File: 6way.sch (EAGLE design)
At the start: 10 parts

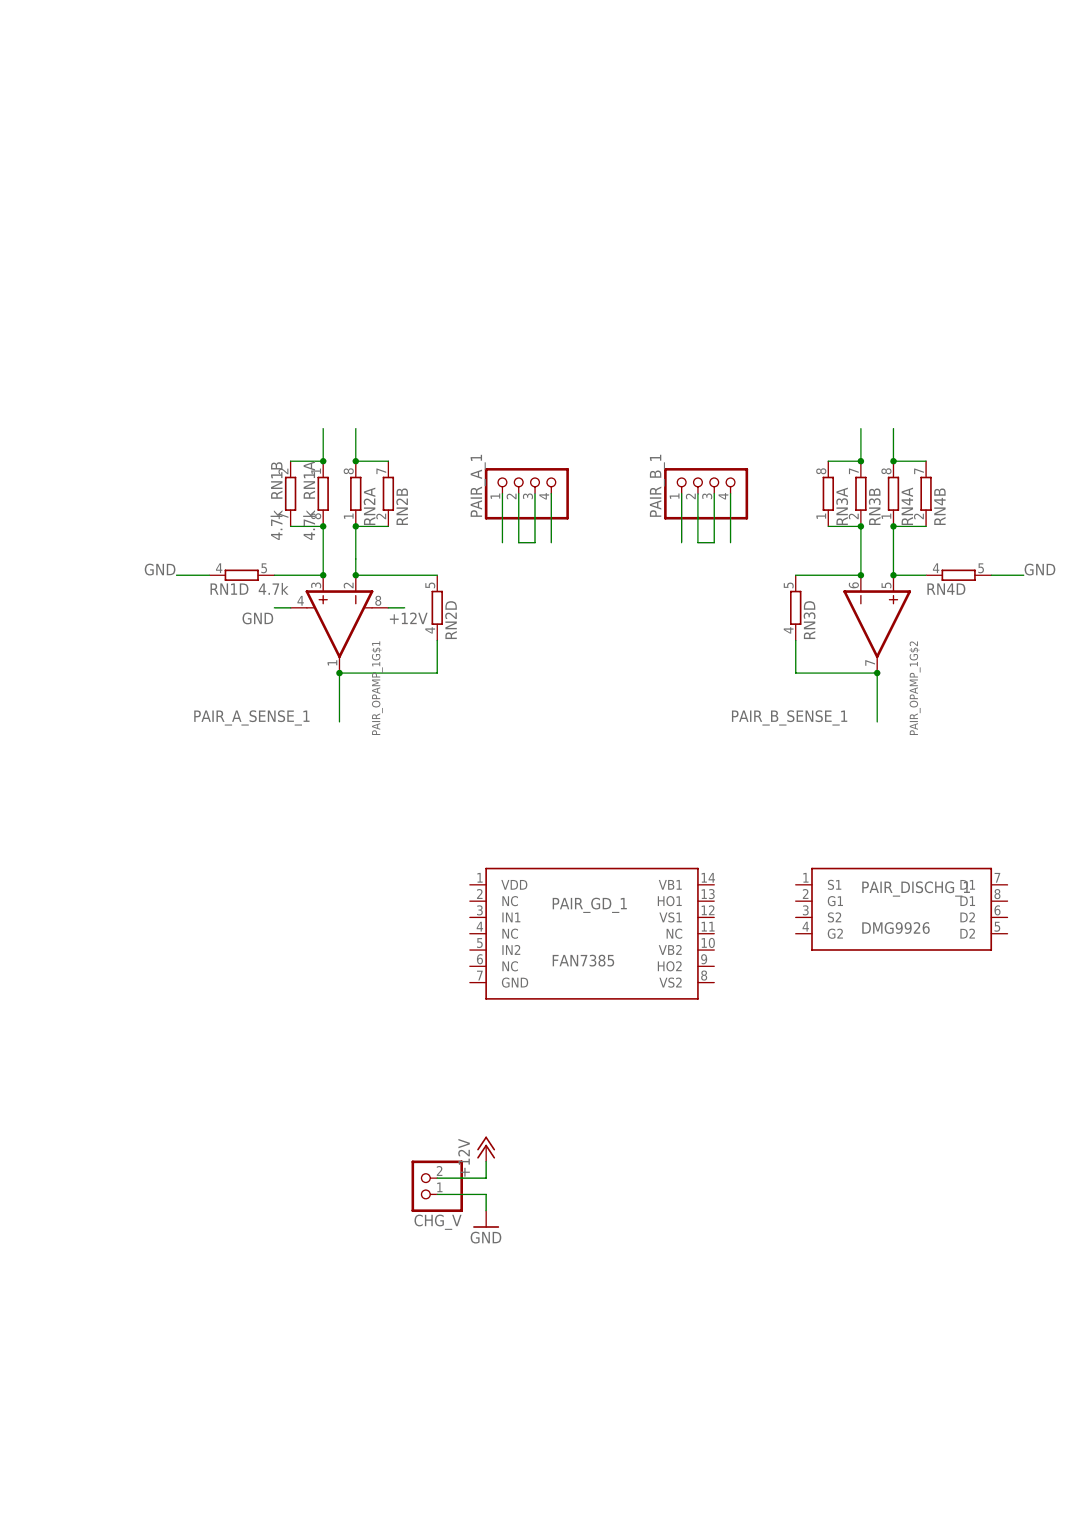
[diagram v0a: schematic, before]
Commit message: wired the signals that I know to handle, next up is figuring out the rest of it, datasheet is a bit sparse on details here
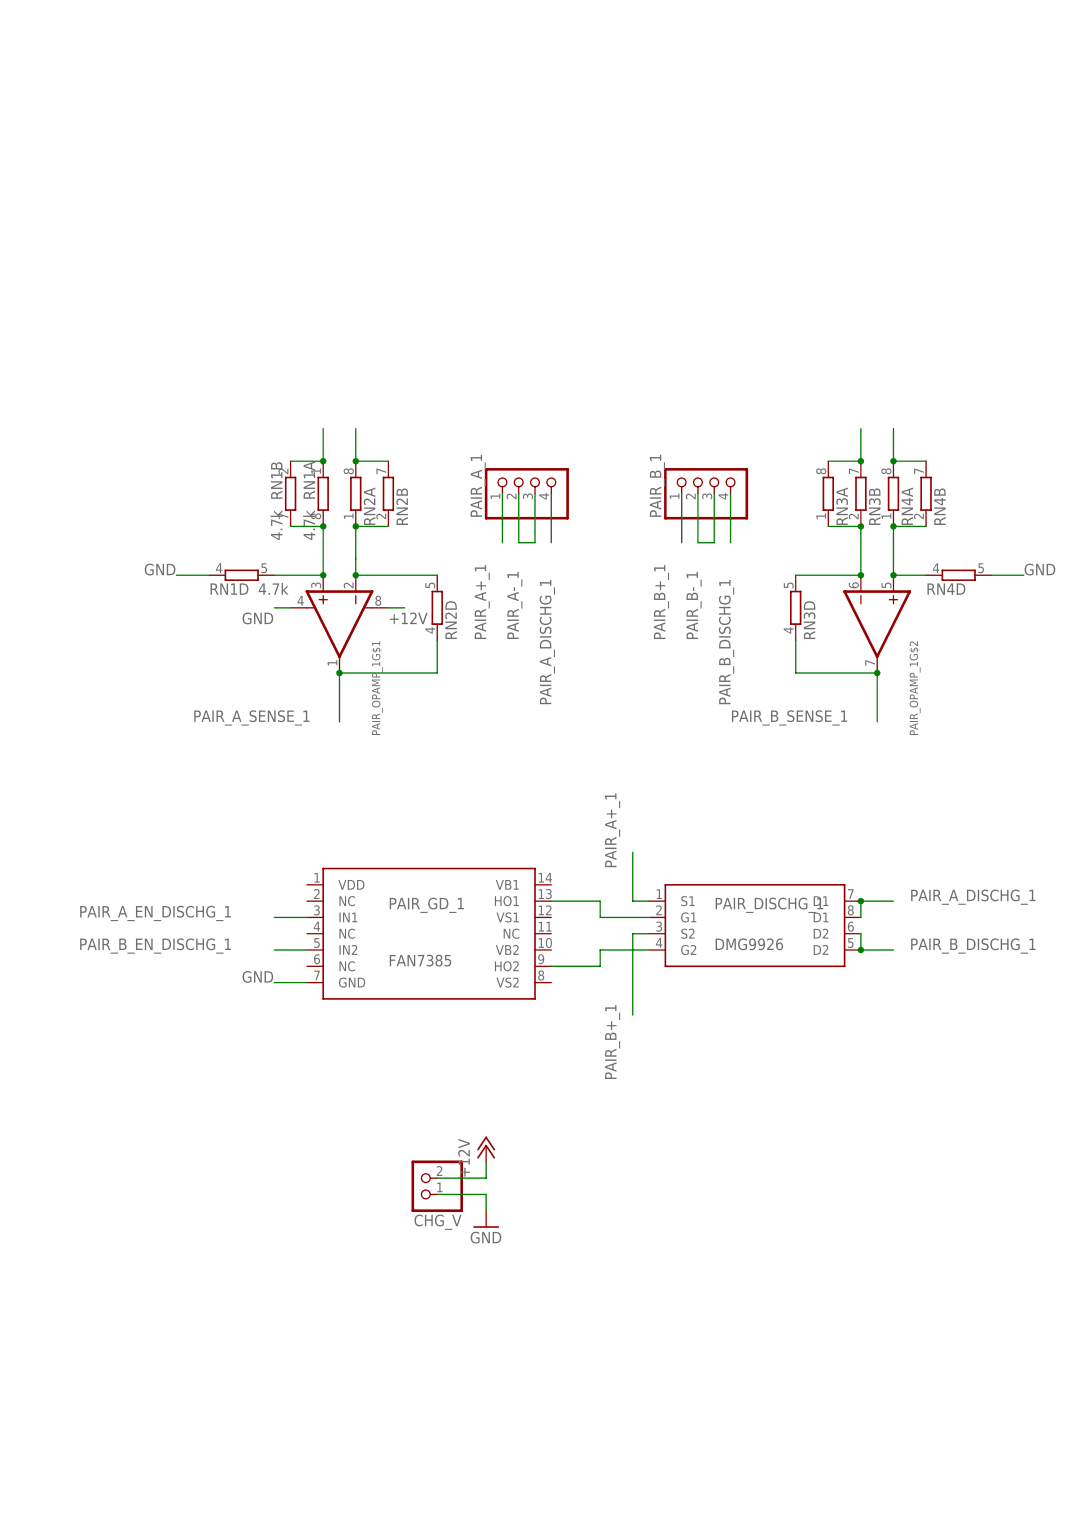
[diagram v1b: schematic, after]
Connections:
- new net N$4: PAIR_DISCHG_1.G1, PAIR_GD_1.HO1
- new net N$6: PAIR_DISCHG_1.G2, PAIR_GD_1.HO2
- new net PAIR_A_EN_DISCHG_1: PAIR_GD_1.IN1
- new net PAIR_B_EN_DISCHG_1: PAIR_GD_1.IN2
- net GND: now also PAIR_GD_1.GND
- net PAIR_A+_1: now also PAIR_DISCHG_1.S1
- net PAIR_A_DISCHG_1: now also PAIR_DISCHG_1.D1@1, PAIR_DISCHG_1.D1@2
- net PAIR_B+_1: now also PAIR_DISCHG_1.S2
- net PAIR_B_DISCHG_1: now also PAIR_DISCHG_1.D2@1, PAIR_DISCHG_1.D2@2
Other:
- moved on the sheet: PAIR_DISCHG_1, PAIR_GD_1
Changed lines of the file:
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@@
 <instance part="RN4" gate="D" x="86.36" y="101.6"/>
 <instance part="PAIR_B_1" gate="A" x="48.26" y="116.84" rot="R90"/>
-<instance part="PAIR_GD_1" gate="G$1" x="25.4" y="45.72"/>
-<instance part="PAIR_DISCHG_1" gate="G$1" x="73.66" y="50.8"/>
+<instance part="PAIR_GD_1" gate="G$1" x="0" y="45.72"/>
+<instance part="PAIR_DISCHG_1" gate="G$1" x="50.8" y="48.26"/>
 </instances>
 <busses>
@@
 <label x="96.52" y="101.6" size="1.778" layer="95"/>
 </segment>
+<segment>
+<pinref part="PAIR_GD_1" gate="G$1" pin="GND"/>
+<wire x1="-15.24" y1="38.1" x2="-20.32" y2="38.1" width="0.1524" layer="91"/>
+<label x="-25.4" y="38.1" size="1.778" layer="95"/>
+</segment>
 </net>
 <net name="PAIR_1_A_+" class="2">
@@
 <wire x1="20.32" y1="114.3" x2="20.32" y2="106.68" width="0.1524" layer="91"/>
 <wire x1="17.78" y1="106.68" x2="20.32" y2="106.68" width="0.1524" layer="91"/>
+<label x="17.78" y="91.44" size="1.778" layer="95" rot="R90"/>
 </segment>
 <segment>
@@
 <pinref part="PAIR_A_1" gate="A" pin="4"/>
 <wire x1="22.86" y1="114.3" x2="22.86" y2="106.68" width="0.1524" layer="91"/>
+<label x="22.86" y="81.28" size="1.778" layer="95" rot="R90"/>
+</segment>
+<segment>
+<pinref part="PAIR_DISCHG_1" gate="G$1" pin="D1@1"/>
+<pinref part="PAIR_DISCHG_1" gate="G$1" pin="D1@2"/>
+<wire x1="71.12" y1="48.26" x2="71.12" y2="50.8" width="0.1524" layer="91"/>
+<wire x1="71.12" y1="50.8" x2="76.2" y2="50.8" width="0.1524" layer="91"/>
+<junction x="71.12" y="50.8"/>
+<label x="78.74" y="50.8" size="1.778" layer="95"/>
 </segment>
 </net>
@@
 <pinref part="PAIR_A_1" gate="A" pin="1"/>
 <wire x1="15.24" y1="114.3" x2="15.24" y2="106.68" width="0.1524" layer="91"/>
+<label x="12.7" y="91.44" size="1.778" layer="95" rot="R90"/>
+</segment>
+<segment>
+<pinref part="PAIR_DISCHG_1" gate="G$1" pin="S1"/>
+<wire x1="38.1" y1="50.8" x2="35.56" y2="50.8" width="0.1524" layer="91"/>
+<wire x1="35.56" y1="50.8" x2="35.56" y2="58.42" width="0.1524" layer="91"/>
+<label x="33.02" y="55.88" size="1.778" layer="95" rot="R90"/>
 </segment>
 </net>
@@
 <wire x1="48.26" y1="114.3" x2="48.26" y2="106.68" width="0.1524" layer="91"/>
 <wire x1="45.72" y1="106.68" x2="48.26" y2="106.68" width="0.1524" layer="91"/>
+<label x="45.72" y="91.44" size="1.778" layer="95" rot="R90"/>
 </segment>
 <segment>
@@
 <pinref part="PAIR_B_1" gate="A" pin="4"/>
 <wire x1="50.8" y1="114.3" x2="50.8" y2="106.68" width="0.1524" layer="91"/>
+<label x="50.8" y="81.28" size="1.778" layer="95" rot="R90"/>
+</segment>
+<segment>
+<pinref part="PAIR_DISCHG_1" gate="G$1" pin="D2@1"/>
+<pinref part="PAIR_DISCHG_1" gate="G$1" pin="D2@2"/>
+<wire x1="71.12" y1="45.72" x2="71.12" y2="43.18" width="0.1524" layer="91"/>
+<wire x1="71.12" y1="43.18" x2="76.2" y2="43.18" width="0.1524" layer="91"/>
+<junction x="71.12" y="43.18"/>
+<label x="78.74" y="43.18" size="1.778" layer="95"/>
 </segment>
 </net>
@@
 <pinref part="PAIR_B_1" gate="A" pin="1"/>
 <wire x1="43.18" y1="114.3" x2="43.18" y2="106.68" width="0.1524" layer="91"/>
+<label x="40.64" y="91.44" size="1.778" layer="95" rot="R90"/>
 </segment>
 <segment>
@@
 <wire x1="76.2" y1="119.38" x2="76.2" y2="124.46" width="0.1524" layer="91"/>
 <junction x="76.2" y="119.38"/>
+</segment>
+<segment>
+<pinref part="PAIR_DISCHG_1" gate="G$1" pin="S2"/>
+<wire x1="38.1" y1="45.72" x2="35.56" y2="45.72" width="0.1524" layer="91"/>
+<wire x1="35.56" y1="45.72" x2="35.56" y2="33.02" width="0.1524" layer="91"/>
+<label x="33.02" y="22.86" size="1.778" layer="95" rot="R90"/>
 </segment>
 </net>
@@
 </segment>
 </net>
+<net name="PAIR_A_EN_DISCHG_1" class="0">
+<segment>
+<pinref part="PAIR_GD_1" gate="G$1" pin="IN1"/>
+<wire x1="-15.24" y1="48.26" x2="-20.32" y2="48.26" width="0.1524" layer="91"/>
+<label x="-50.8" y="48.26" size="1.778" layer="95"/>
+</segment>
+</net>
+<net name="PAIR_B_EN_DISCHG_1" class="0">
+<segment>
+<pinref part="PAIR_GD_1" gate="G$1" pin="IN2"/>
+<wire x1="-15.24" y1="43.18" x2="-20.32" y2="43.18" width="0.1524" layer="91"/>
+<label x="-50.8" y="43.18" size="1.778" layer="95"/>
+</segment>
+</net>
+<net name="N$4" class="0">
+<segment>
+<pinref part="PAIR_GD_1" gate="G$1" pin="HO1"/>
+<wire x1="22.86" y1="50.8" x2="30.48" y2="50.8" width="0.1524" layer="91"/>
+<wire x1="30.48" y1="50.8" x2="30.48" y2="48.26" width="0.1524" layer="91"/>
+<pinref part="PAIR_DISCHG_1" gate="G$1" pin="G1"/>
+<wire x1="30.48" y1="48.26" x2="38.1" y2="48.26" width="0.1524" layer="91"/>
+</segment>
+</net>
+<net name="N$6" class="0">
+<segment>
+<pinref part="PAIR_GD_1" gate="G$1" pin="HO2"/>
+<wire x1="22.86" y1="40.64" x2="30.48" y2="40.64" width="0.1524" layer="91"/>
+<wire x1="30.48" y1="40.64" x2="30.48" y2="43.18" width="0.1524" layer="91"/>
+<pinref part="PAIR_DISCHG_1" gate="G$1" pin="G2"/>
+<wire x1="30.48" y1="43.18" x2="38.1" y2="43.18" width="0.1524" layer="91"/>
+</segment>
+</net>

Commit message: this I still knew how to do
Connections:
- net PAIR_A+_1: now also PAIR_GD_1.VDD
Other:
- note added: "The "A" cap is the "high" side of a pair"
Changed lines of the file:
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@@
 <sheet>
 <plain>
+<text x="2.54" y="127" size="1.778" layer="91">The "A" cap is the "high" side of a pair</text>
 </plain>
 <instances>
@@
 <label x="33.02" y="55.88" size="1.778" layer="95" rot="R90"/>
 </segment>
+<segment>
+<pinref part="PAIR_GD_1" gate="G$1" pin="VDD"/>
+<wire x1="-15.24" y1="53.34" x2="-20.32" y2="53.34" width="0.1524" layer="91"/>
+<label x="-35.56" y="53.34" size="1.778" layer="95"/>
+</segment>
 </net>
